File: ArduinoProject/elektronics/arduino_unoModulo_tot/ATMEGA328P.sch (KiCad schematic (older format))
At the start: 9 parts, among them SW1 RESET_SWITCH, U5 ATMEGA328P, X2 CSTCE16MOV53-R0

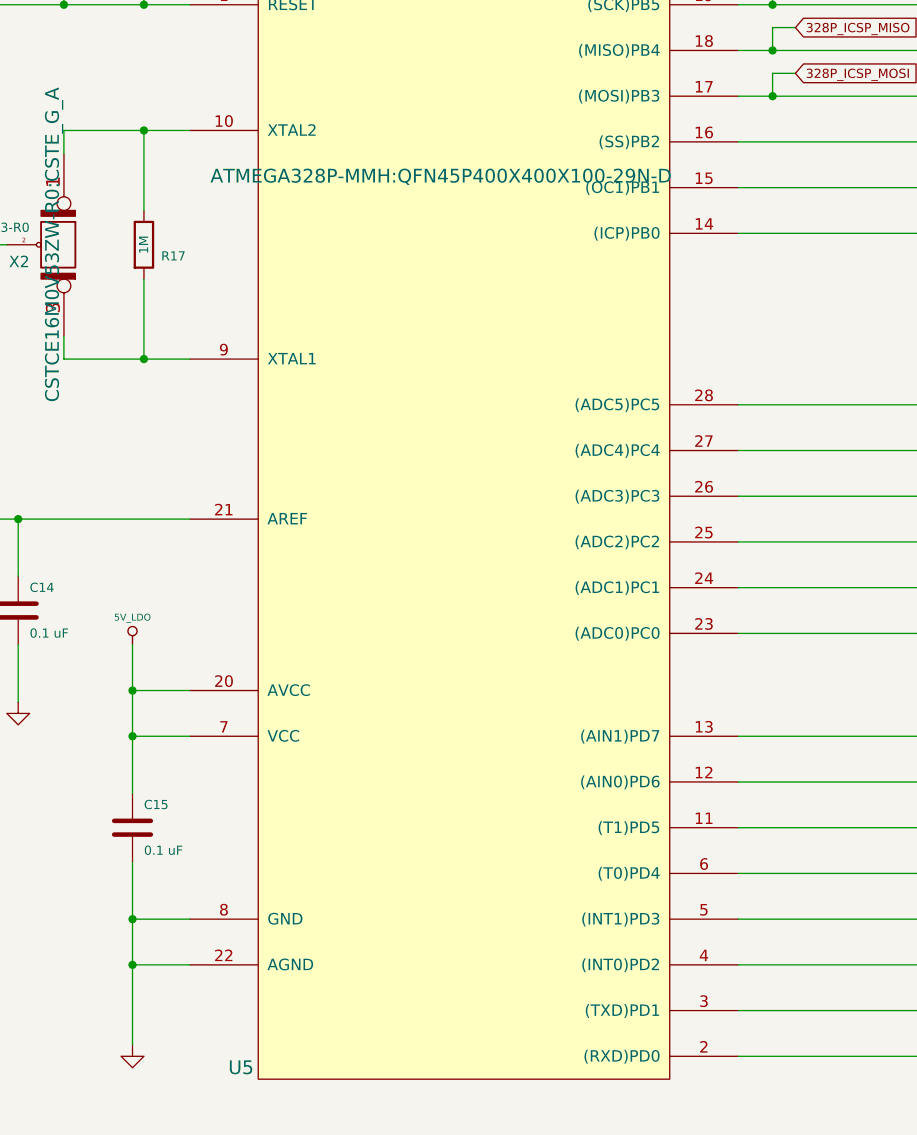
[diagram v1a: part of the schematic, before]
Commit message: kicad schema altered: alles op 1 PCB
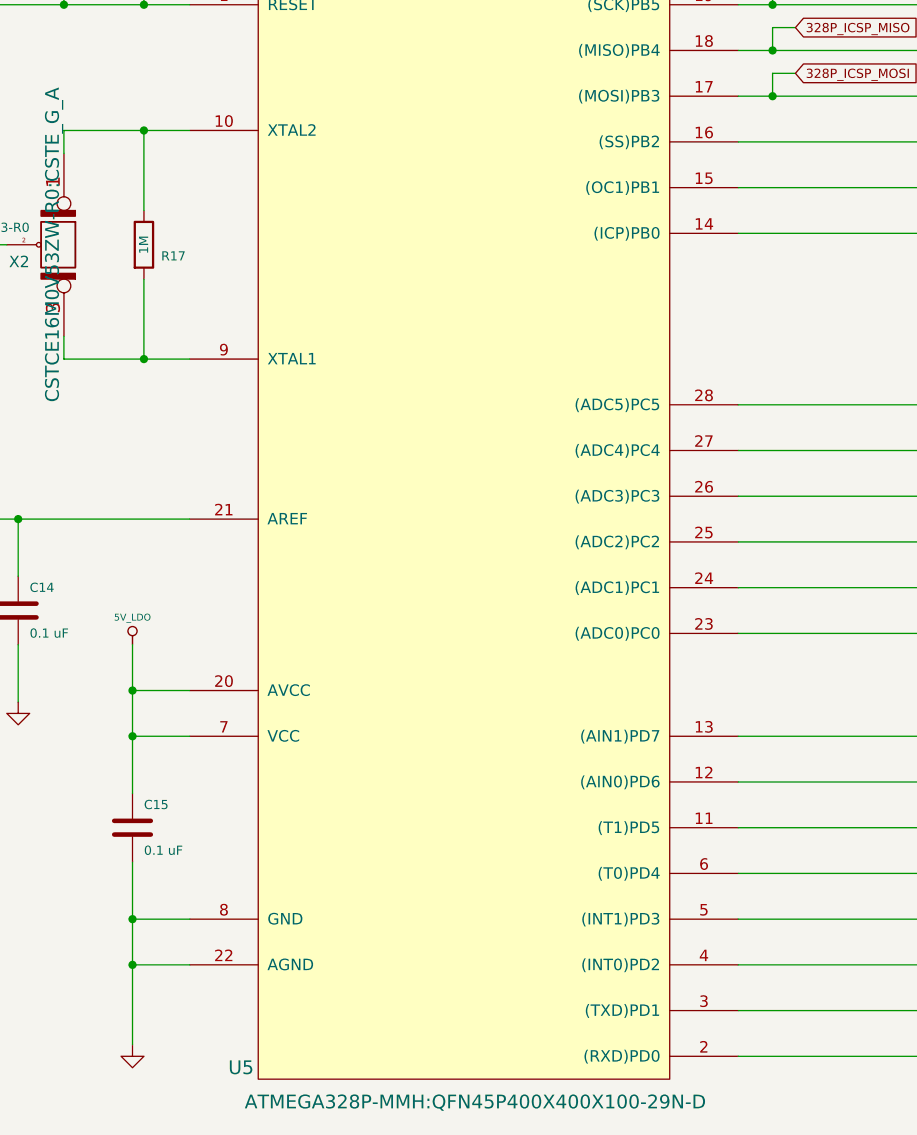
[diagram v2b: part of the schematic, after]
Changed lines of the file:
@@
 LIBS:MFN_STMicro
 LIBS:Arduino_Uno_R3_From_Scratch-cache
-LIBS:L298_Driver-cache
 EELAYER 25 0
 EELAYER END
 $Descr A4 11693 8268
 encoding utf-8
-Sheet 5 6
+Sheet 3 6
 Title "Arduino UNO R3 Clone"
 Date "8 oct 2015"
@@
 F 0 "U5" H 6075 1350 60  0000 C CNN
 F 1 "ATMEGA328P" H 7050 6300 60  0000 C CNN
-F 2 "ATMEGA328P-MMH:QFN45P400X400X100-29N-D" H 6950 5250 60  0000 C CNN
+F 2 "ATMEGA328P-MMH:QFN45P400X400X100-29N-D" H 7100 1200 60  0000 C CNN
 F 3 "http://www.atmel.com/images/Atmel-8271-8-bit-AVR-Microcontroller-ATmega48A-48PA-88A-88PA-168A-168PA-328-328P_datasheet_Complete.pdf" H 6950 5250 60  0001 C CNN
 F 4 "IC MCU 8BIT 32KB FLASH 28DIP" H 7050 3750 60  0001 C CNN "Characteristics"
@@
 	4800 3750 5850 3750
 $Comp
-L GND #PWR020
+L GND #PWR06
 U 1 1 55E8AA8C
 P 5600 6050
-F 0 "#PWR020" H 5600 6050 30  0001 C CNN
+F 0 "#PWR06" H 5600 6050 30  0001 C CNN
 F 1 "GND" H 5600 5980 30  0001 C CNN
 F 2 "~" H 5600 6050 60  0000 C CNN
@@
 	3200 950  3200 1500
 $Comp
-L 5V_LDO #PWR021
+L 5V_LDO #PWR07
 U 1 1 55E95BB4
 P 4900 650
-F 0 "#PWR021" H 4900 740 20  0001 C CNN
+F 0 "#PWR07" H 4900 740 20  0001 C CNN
 F 1 "5V_LDO" H 4900 770 30  0000 C CNN
 F 2 "~" H 4900 650 60  0000 C CNN
@@
 $EndComp
 $Comp
-L 5V_LDO #PWR022
+L 5V_LDO #PWR08
 U 1 1 55E95BC3
 P 5600 4300
-F 0 "#PWR022" H 5600 4390 20  0001 C CNN
+F 0 "#PWR08" H 5600 4390 20  0001 C CNN
 F 1 "5V_LDO" H 5600 4420 30  0000 C CNN
 F 2 "~" H 5600 4300 60  0000 C CNN
@@
 	3300 2275 3300 2175
 $Comp
-L GND #PWR023
+L GND #PWR09
 U 1 1 562077A6
 P 5100 4550
-F 0 "#PWR023" H 5100 4550 30  0001 C CNN
+F 0 "#PWR09" H 5100 4550 30  0001 C CNN
 F 1 "GND" H 5100 4480 30  0001 C CNN
 F 2 "~" H 5100 4550 60  0000 C CNN
@@
 $EndComp
 $Comp
-L GND #PWR024
+L GND #PWR010
 U 1 1 56207870
 P 4750 2900
-F 0 "#PWR024" H 4750 2900 30  0001 C CNN
+F 0 "#PWR010" H 4750 2900 30  0001 C CNN
 F 1 "GND" H 4750 2830 30  0001 C CNN
 F 2 "~" H 4750 2900 60  0000 C CNN
@@
 $EndComp
 $Comp
-L GND #PWR025
+L GND #PWR011
 U 1 1 562079B8
 P 3400 2425
-F 0 "#PWR025" H 3400 2425 30  0001 C CNN
+F 0 "#PWR011" H 3400 2425 30  0001 C CNN
 F 1 "GND" H 3400 2355 30  0001 C CNN
 F 2 "~" H 3400 2425 60  0000 C CNN
@@
 $EndComp
 $Comp
-L GND #PWR026
+L GND #PWR012
 U 1 1 56208C49
 P 4350 1100
-F 0 "#PWR026" H 4350 1100 30  0001 C CNN
+F 0 "#PWR012" H 4350 1100 30  0001 C CNN
 F 1 "GND" H 4350 1030 30  0001 C CNN
 F 2 "~" H 4350 1100 60  0000 C CNN

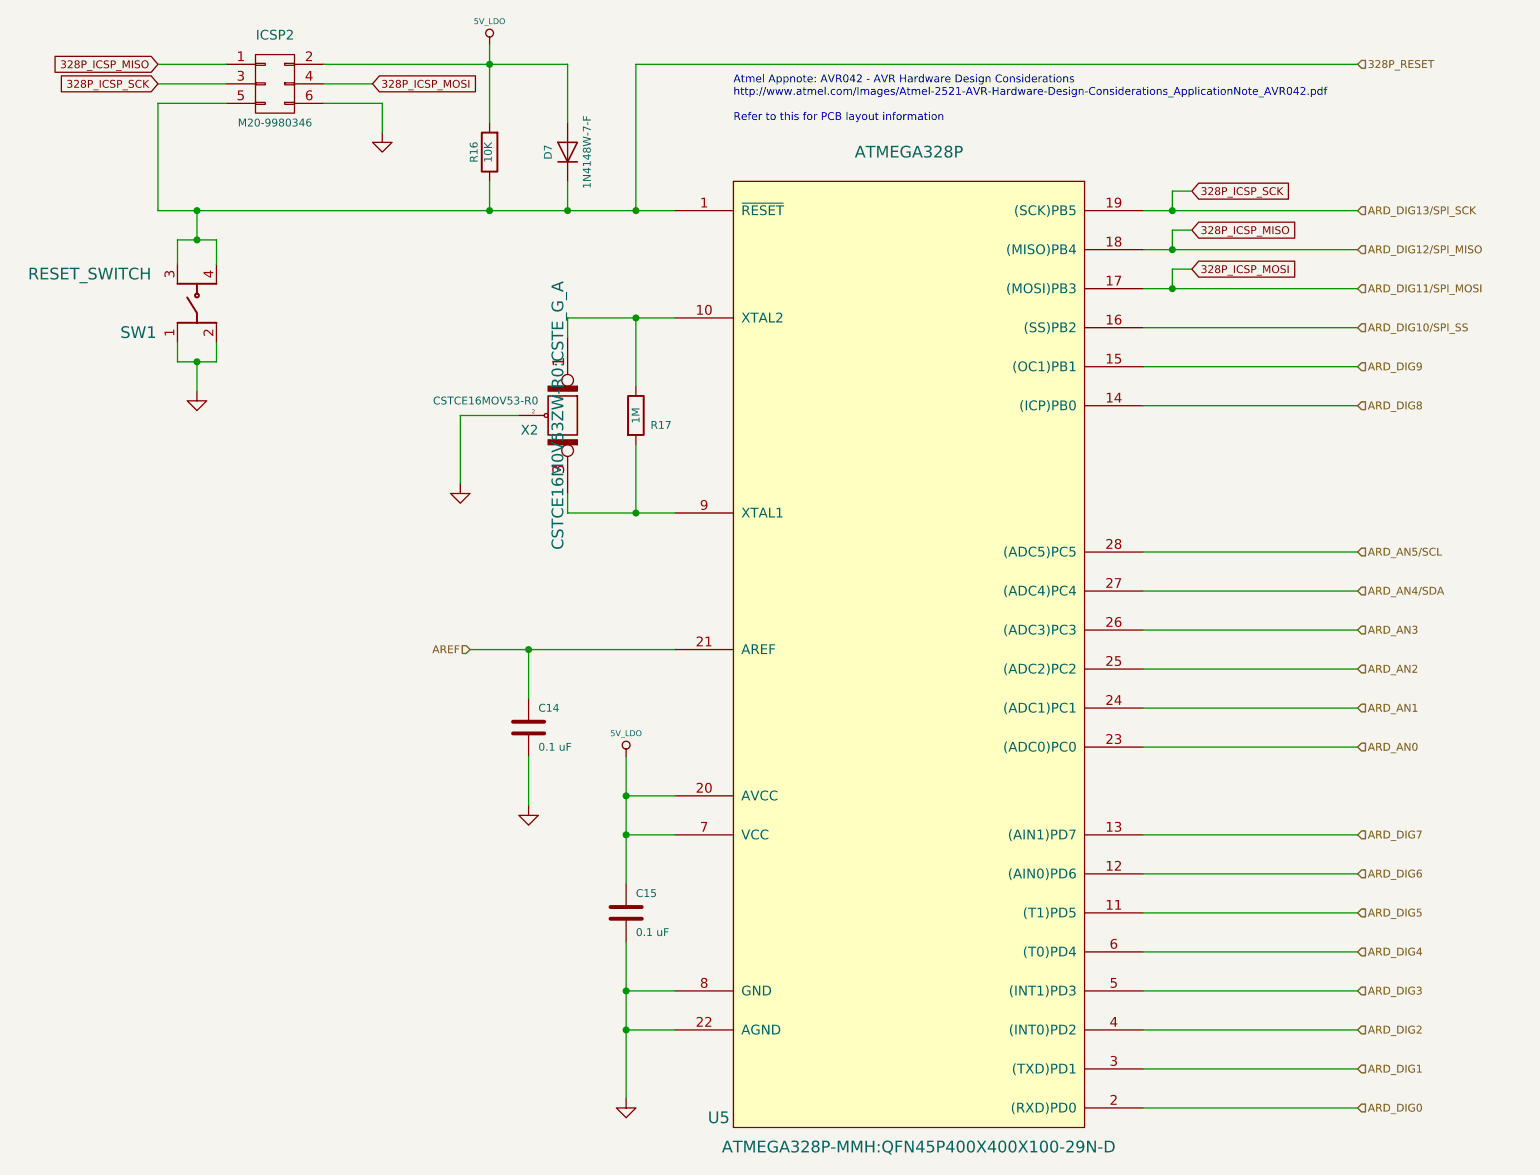
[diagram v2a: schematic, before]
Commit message: kicad schema altered: alles op 1 PCB2
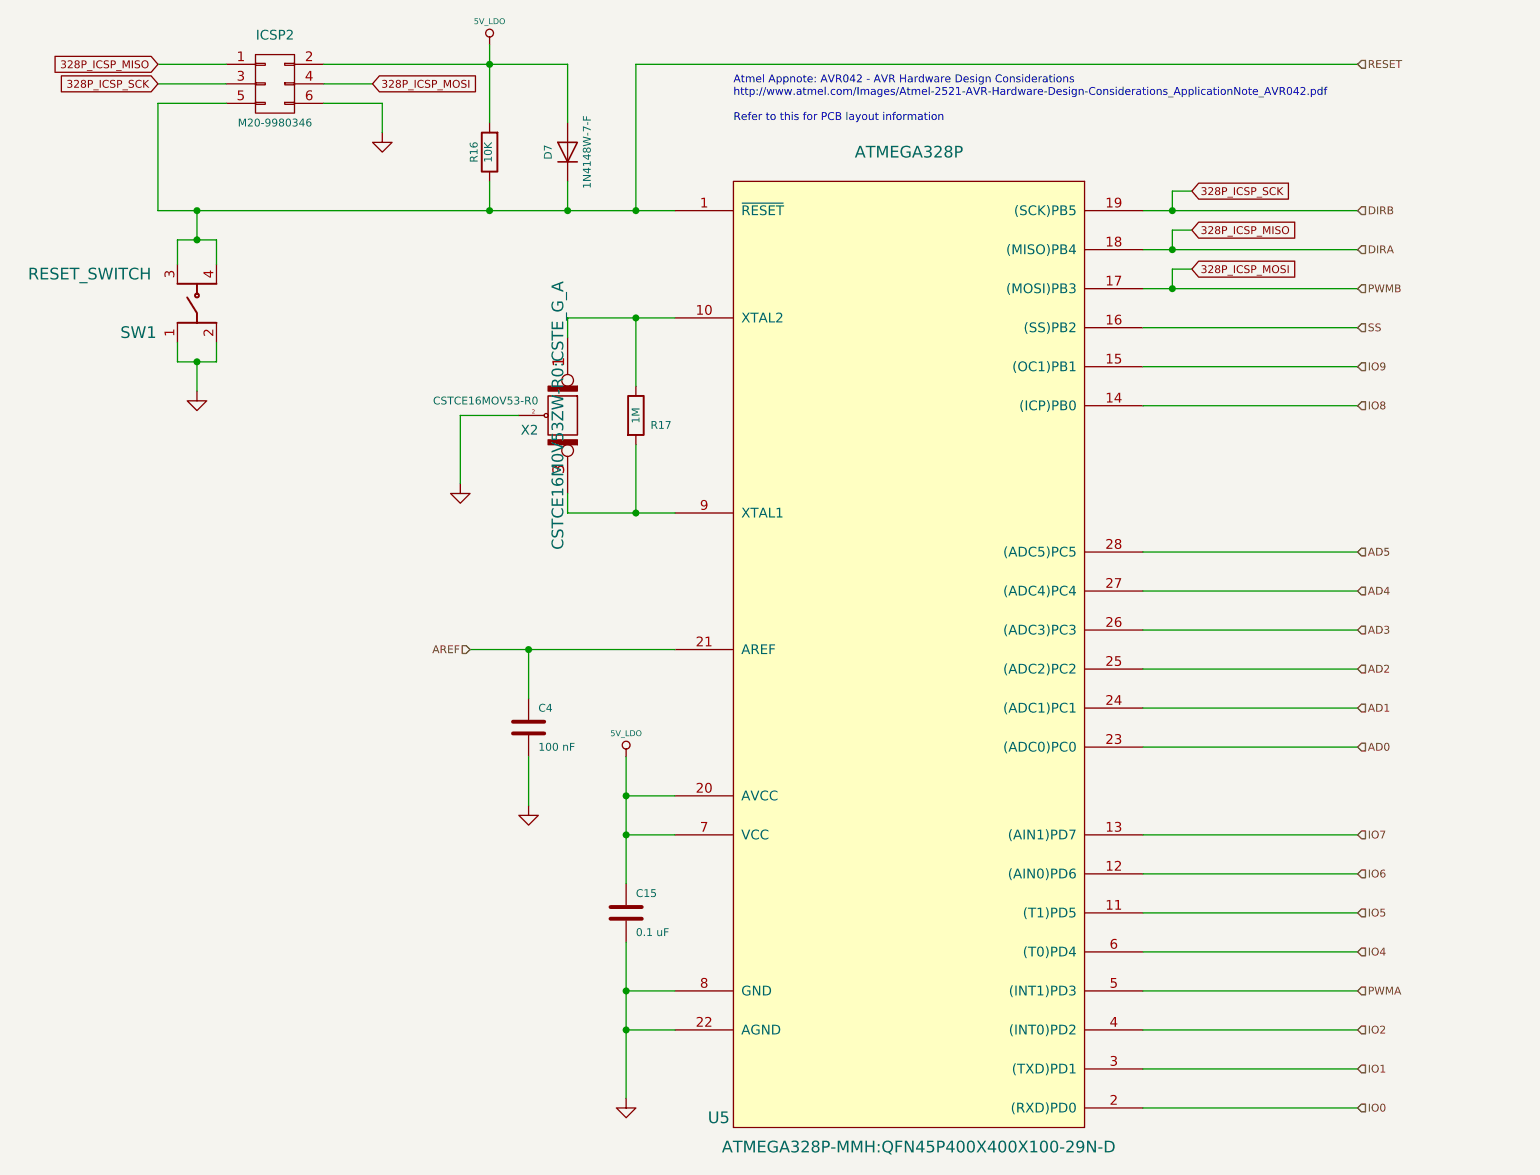
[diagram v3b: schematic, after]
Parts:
- C4: renamed from C14; value 0.1 uF -> 100 nF
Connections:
- net 328P_RESET renamed RESET
- net ARD_AN0 renamed AD0
- net ARD_AN1 renamed AD1
- net ARD_AN2 renamed AD2
- net ARD_AN3 renamed AD3
- net ARD_AN4/SDA renamed AD4
- net ARD_AN5/SCL renamed AD5
- net ARD_DIG0 renamed IO0
- net ARD_DIG1 renamed IO1
- net ARD_DIG10/SPI_SS renamed SS
- net ARD_DIG2 renamed IO2
- net ARD_DIG3 renamed PWMA
- net ARD_DIG4 renamed IO4
- net ARD_DIG5 renamed IO5
- net ARD_DIG6 renamed IO6
- net ARD_DIG7 renamed IO7
- net ARD_DIG8 renamed IO8
- net ARD_DIG9 renamed IO9
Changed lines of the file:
@@
 $Descr A4 11693 8268
 encoding utf-8
-Sheet 3 6
+Sheet 6 6
 Title "Arduino UNO R3 Clone"
 Date "8 oct 2015"
@@
 	8250 5900 9350 5900
 Text HLabel 9350 3250 2    40   Input ~ 0
-ARD_AN5/SCL
+AD5
 Text HLabel 9350 3450 2    40   Input ~ 0
-ARD_AN4/SDA
+AD4
 Text HLabel 9350 3650 2    40   Input ~ 0
-ARD_AN3
+AD3
 Text HLabel 9350 3850 2    40   Input ~ 0
-ARD_AN2
+AD2
 Text HLabel 9350 4050 2    40   Input ~ 0
-ARD_AN1
+AD1
 Text HLabel 9350 4250 2    40   Input ~ 0
-ARD_AN0
+AD0
 Wire Wire Line
 	9350 3250 8250 3250
@@
 	8250 4250 9350 4250
 Text HLabel 9350 4700 2    40   Input ~ 0
-ARD_DIG7
+IO7
 Text HLabel 9350 4900 2    40   Input ~ 0
-ARD_DIG6
+IO6
 Text HLabel 9350 5100 2    40   Input ~ 0
-ARD_DIG5
+IO5
 Text HLabel 9350 5300 2    40   Input ~ 0
-ARD_DIG4
+IO4
 Text HLabel 9350 5500 2    40   Input ~ 0
-ARD_DIG3
+PWMA
 Text HLabel 9350 5700 2    40   Input ~ 0
-ARD_DIG2
+IO2
 Text HLabel 9350 5900 2    40   Input ~ 0
-ARD_DIG1
+IO1
 Text HLabel 9350 6100 2    40   Input ~ 0
-ARD_DIG0
+IO0
 Wire Wire Line
 	8250 5700 9350 5700
@@
 	9350 4700 8250 4700
 Text HLabel 9350 2500 2    40   Input ~ 0
-ARD_DIG8
+IO8
 Text HLabel 9350 2300 2    40   Input ~ 0
-ARD_DIG9
+IO9
 Text HLabel 9350 2100 2    40   Input ~ 0
-ARD_DIG10/SPI_SS
+SS
 Text HLabel 9350 1900 2    40   Input ~ 0
-ARD_DIG11/SPI_MOSI
+PWMB
 Text HLabel 9350 1700 2    40   Input ~ 0
-ARD_DIG12/SPI_MISO
+DIRA
 Text HLabel 9350 1500 2    40   Input ~ 0
-ARD_DIG13/SPI_SCK
+DIRB
 Wire Wire Line
 	9350 2500 8250 2500
@@
 	8250 1500 9350 1500
 Text HLabel 9350 750  2    40   Input ~ 0
-328P_RESET
+RESET
 Wire Wire Line
 	3200 1500 5850 1500
@@
 Atmel Appnote: AVR042 - AVR Hardware Design Considerations\nhttp://www.atmel.com/Images/Atmel-2521-AVR-Hardware-Design-Considerations_ApplicationNote_AVR042.pdf\n\nRefer to this for PCB layout information
 $Comp
-L C C14
+L C C4
 U 1 1 56159BB8
 P 5100 4150
-F 0 "C14" H 5150 4250 40  0000 L CNN
-F 1 "0.1 uF" H 5150 4050 40  0000 L CNN
+F 0 "C4" H 5150 4250 40  0000 L CNN
+F 1 "100 nF" H 5150 4050 40  0000 L CNN
 F 2 "" H 5138 4000 30  0001 C CNN
 F 3 "http://images.ihscontent.net/vipimages/VipMasterIC/IC/KEME/KEMES10043/KEMES10043-1.pdf" H 5100 4150 60  0001 C CNN
